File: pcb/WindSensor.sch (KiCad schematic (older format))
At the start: 13 parts, among them P1 SP, P2 0V, P3 3v3, P4 SP, P5 SDA, P6 SCL, P7 5V, P8 GND, P9 GND, U1 ArdinoMinPro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

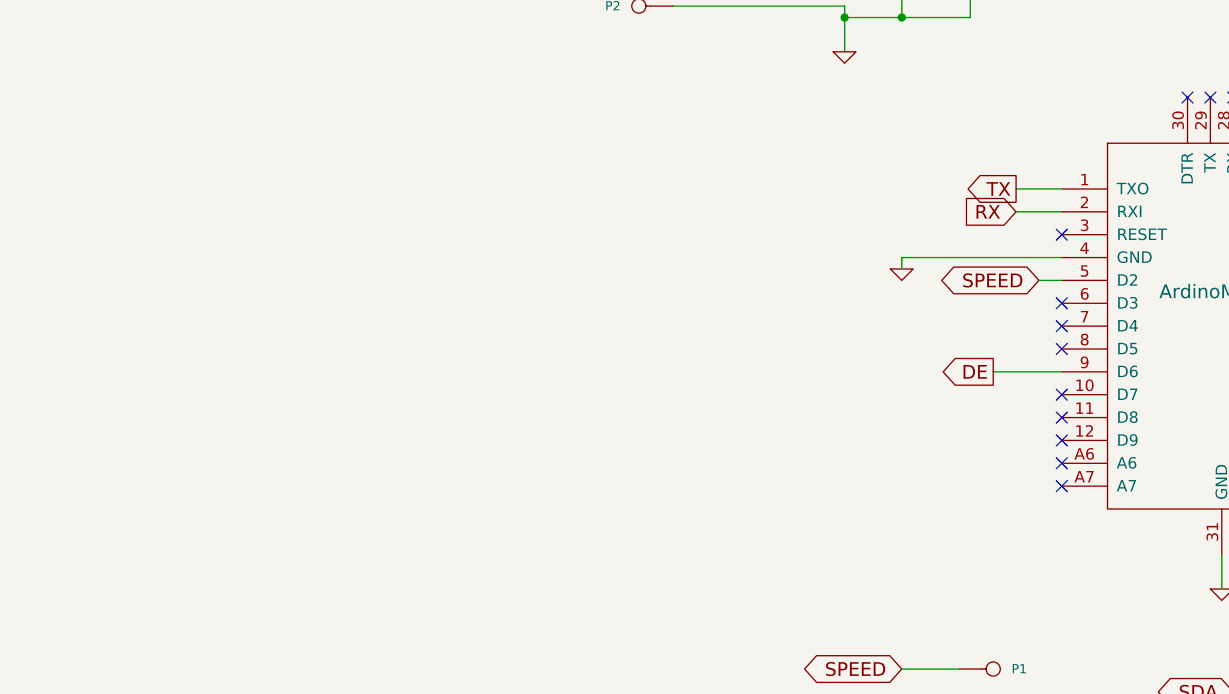
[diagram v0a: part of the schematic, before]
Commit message: Modularised the libraries and added unit tests, updated pcb, working version
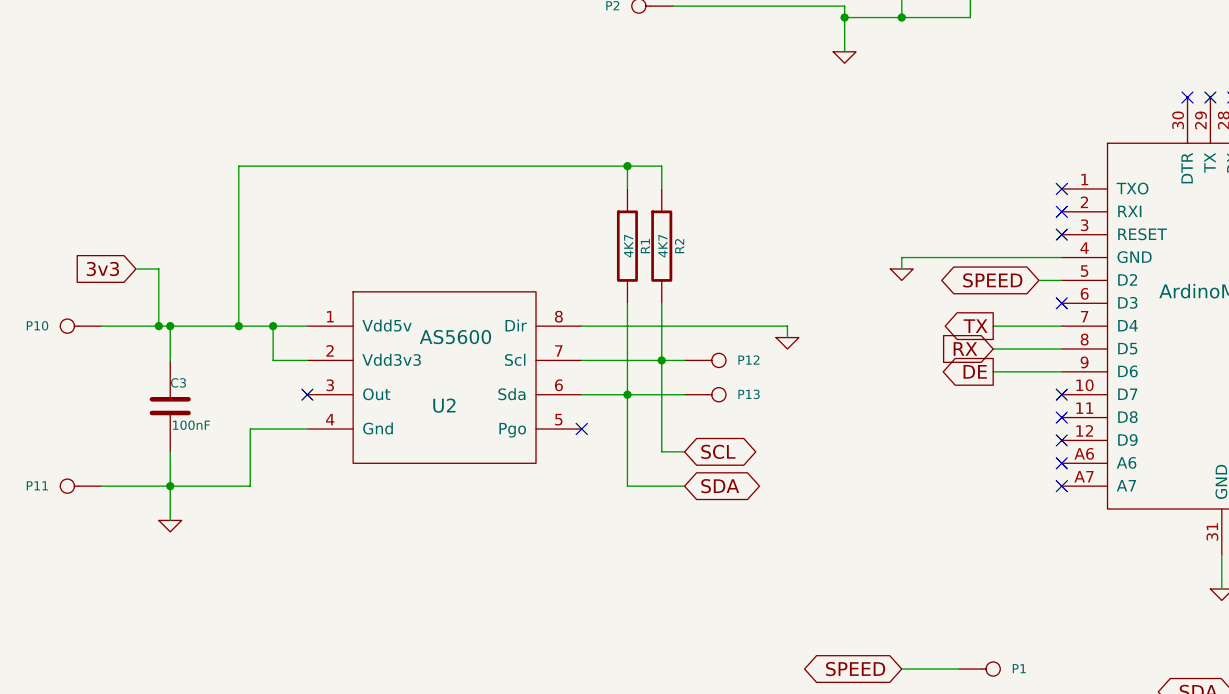
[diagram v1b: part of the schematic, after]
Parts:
- added C3: 100nF, Capacitors_SMD:C_0805, symbol C
- added P10: 3v3, Wire_Pads:SolderWirePad_single_0-8mmDrill, symbol CONN_1
- added P11: GND, Wire_Pads:SolderWirePad_single_0-8mmDrill, symbol CONN_1
- added P12: SDA, Wire_Pads:SolderWirePad_single_0-8mmDrill, symbol CONN_1
- added P13: SCL, Wire_Pads:SolderWirePad_single_0-8mmDrill, symbol CONN_1
- added R1, R2: 4K7, Capacitors_SMD:C_0805, symbol R
- added U2: AS5600, SMD_Packages:SOIC-8-N, symbol AS5600
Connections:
- net 3v3: now also C3.1, P10.1, R1.1, R2.1, U2.1 (Vdd5v), U2.2 (Vdd3v3)
- net GND: now also C3.2, P11.1, U2.4 (Gnd), U2.8 (Dir)
- net RX: now also U1.8 (D5); no longer U1.2 (RXI)
- net SCL: now also P12.1, R2.2, U2.7 (Scl)
- net SDA: now also P13.1, R1.2, U2.6 (Sda)
- net TX: now also U1.7 (D4); no longer U1.1 (TXO)
- no-connect marks 31 -> 33
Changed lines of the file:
@@
 Text GLabel 6750 4550 2    60   BiDi ~ 0
 SDA
-Text GLabel 4800 3350 0    60   Output ~ 0
+Text GLabel 4700 3950 0    60   Output ~ 0
 TX
-Text GLabel 4800 3450 0    60   Input ~ 0
+Text GLabel 4700 4050 0    60   Input ~ 0
 RX
 Text GLabel 4700 4150 0    60   Output ~ 0
@@
 NoConn ~ 5750 2950
 NoConn ~ 5850 2950
-NoConn ~ 5000 3950
-Wire Wire Line
-	6500 3450 6850 3450
-Wire Wire Line
-	6850 3450 6850 3500
-Wire Wire Line
-	4300 3650 5000 3650
-Wire Wire Line
-	6800 3650 6500 3650
-Wire Wire Line
-	5000 3750 4900 3750
-Wire Wire Line
-	4300 3650 4300 3700
-Wire Wire Line
-	6750 4550 6500 4550
-Wire Wire Line
-	6500 4650 6750 4650
-Wire Wire Line
-	9700 3500 9850 3500
-Wire Wire Line
-	9700 3600 9850 3600
-Wire Wire Line
-	9700 3200 10250 3200
-Wire Wire Line
-	9800 3200 9800 3300
-Wire Wire Line
-	9800 3300 9700 3300
-Wire Wire Line
-	9850 3400 9700 3400
-Wire Wire Line
-	9850 3700 9700 3700
-Wire Wire Line
-	10250 3200 10250 3300
-Connection ~ 9800 3200
-Wire Wire Line
-	6500 3350 6950 3350
-Wire Wire Line
-	4600 2600 4600 2450
-Wire Wire Line
-	4050 2600 4600 2600
-Wire Wire Line
-	4050 2550 4050 2750
-Wire Wire Line
-	4300 2450 4300 2600
-Connection ~ 4300 2600
-Wire Wire Line
-	3050 1900 4850 1900
-Wire Wire Line
-	4600 1900 4600 2050
-Wire Wire Line
-	4300 2050 4300 1900
-Connection ~ 4300 1900
-Wire Wire Line
-	3300 2550 4050 2550
-Connection ~ 4050 2600
-Wire Wire Line
-	6150 5250 6000 5250
-Connection ~ 4600 1900
-Wire Wire Line
-	6050 2950 6050 2850
-Wire Wire Line
-	5950 2850 6350 2850
-Wire Wire Line
-	6350 2850 6350 2950
-Wire Wire Line
-	5950 2850 5950 2950
-Connection ~ 6050 2850
-Wire Wire Line
-	5700 4950 5700 5100
-Wire Wire Line
-	5000 3450 4800 3450
-Wire Wire Line
-	5000 3350 4800 3350
 NoConn ~ 5000 3850
 $Comp
@@
 	1    0    0    -1
 $EndComp
-Wire Wire Line
-	4300 5450 4550 5450
 NoConn ~ 5000 4250
 $Comp
@@
 	1    0    0    -1
 $EndComp
-Wire Wire Line
-	4700 4150 5000 4150
-NoConn ~ 5000 4050
 Text GLabel 5750 5550 0    60   BiDi ~ 0
 SDA
@@
 	1    0    0    -1
 $EndComp
-Wire Wire Line
-	5750 5550 6000 5550
-Wire Wire Line
-	5750 5700 6000 5700
 $Comp
 L GND #PWR07
@@
 	1    0    0    -1
 $EndComp
-Wire Wire Line
-	5600 6050 5600 5950
-Wire Wire Line
-	5600 5950 6000 5950
 Text GLabel 4300 5650 0    60   Input ~ 0
 5V
@@
 	1    0    0    -1
 $EndComp
-Wire Wire Line
-	4300 5650 4550 5650
 $Comp
 L GND #PWR08
@@
 	1    0    0    -1
 $EndComp
+NoConn ~ 5000 3450
+NoConn ~ 5000 3350
+$Comp
+L AS5600 U2
+U 1 1 5FE9996D
+P 2300 4300
+F 0 "U2" H 2300 4300 60  0000 C CNN
+F 1 "AS5600" H 2350 4600 60  0000 C CNN
+F 2 "SMD_Packages:SOIC-8-N" H 2300 4300 60  0001 C CNN
+F 3 "" H 2300 4300 60  0001 C CNN
+	1    2300 4300
+	1    0    0    -1
+$EndComp
+Text GLabel 3350 4650 2    60   BiDi ~ 0
+SDA
+Text GLabel 3350 4500 2    60   BiDi ~ 0
+SCL
+NoConn ~ 1700 4250
+NoConn ~ 2900 4400
+$Comp
+L C C3
+U 1 1 5FE99E5F
+P 1100 4300
+F 0 "C3" H 1100 4400 40  0000 L CNN
+F 1 "100nF" H 1106 4215 40  0000 L CNN
+F 2 "Capacitors_SMD:C_0805" H 1138 4150 30  0001 C CNN
+F 3 "" H 1100 4300 60  0000 C CNN
+	1    1100 4300
+	1    0    0    -1
+$EndComp
+$Comp
+L GND #PWR09
+U 1 1 5FE99F11
+P 1100 4800
+F 0 "#PWR09" H 1100 4800 30  0001 C CNN
+F 1 "GND" H 1100 4730 30  0001 C CNN
+F 2 "" H 1100 4800 60  0001 C CNN
+F 3 "" H 1100 4800 60  0001 C CNN
+	1    1100 4800
+	1    0    0    -1
+$EndComp
+$Comp
+L R R2
+U 1 1 5FE9A09C
+P 3250 3600
+F 0 "R2" V 3330 3600 40  0000 C CNN
+F 1 "4K7" V 3257 3601 40  0000 C CNN
+F 2 "Capacitors_SMD:C_0805" V 3180 3600 30  0001 C CNN
+F 3 "" H 3250 3600 30  0000 C CNN
+	1    3250 3600
+	1    0    0    -1
+$EndComp
+$Comp
+L R R1
+U 1 1 5FE9A16A
+P 3100 3600
+F 0 "R1" V 3180 3600 40  0000 C CNN
+F 1 "4K7" V 3107 3601 40  0000 C CNN
+F 2 "Capacitors_SMD:C_0805" V 3030 3600 30  0001 C CNN
+F 3 "" H 3100 3600 30  0000 C CNN
+	1    3100 3600
+	1    0    0    -1
+$EndComp
+$Comp
+L GND #PWR010
+U 1 1 5FE9A1F6
+P 3800 4000
+F 0 "#PWR010" H 3800 4000 30  0001 C CNN
+F 1 "GND" H 3800 3930 30  0001 C CNN
+F 2 "" H 3800 4000 60  0001 C CNN
+F 3 "" H 3800 4000 60  0001 C CNN
+	1    3800 4000
+	1    0    0    -1
+$EndComp
+$Comp
+L CONN_1 P10
+U 1 1 5FE9A696
+P 650 3950
+F 0 "P10" H 730 3950 40  0000 L CNN
+F 1 "3v3" H 650 4005 30  0001 C CNN
+F 2 "Wire_Pads:SolderWirePad_single_0-8mmDrill" H 650 3950 60  0001 C CNN
+F 3 "" H 650 3950 60  0001 C CNN
+	1    650  3950
+	-1   0    0    1
+$EndComp
+Text GLabel 950  3700 0    60   Input ~ 0
+3v3
+$Comp
+L CONN_1 P12
+U 1 1 5FE9A6A0
+P 3500 4100
+F 0 "P12" H 3580 4100 40  0000 L CNN
+F 1 "SDA" H 3500 4155 30  0001 C CNN
+F 2 "Wire_Pads:SolderWirePad_single_0-8mmDrill" H 3500 4100 60  0001 C CNN
+F 3 "" H 3500 4100 60  0001 C CNN
+	1    3500 4100
+	1    0    0    -1
+$EndComp
+$Comp
+L CONN_1 P13
+U 1 1 5FE9A6A6
+P 3500 4250
+F 0 "P13" H 3580 4250 40  0000 L CNN
+F 1 "SCL" H 3500 4305 30  0001 C CNN
+F 2 "Wire_Pads:SolderWirePad_single_0-8mmDrill" H 3500 4250 60  0001 C CNN
+F 3 "" H 3500 4250 60  0001 C CNN
+	1    3500 4250
+	1    0    0    -1
+$EndComp
+$Comp
+L CONN_1 P11
+U 1 1 5FE9A6B4
+P 650 4650
+F 0 "P11" H 730 4650 40  0000 L CNN
+F 1 "GND" H 650 4705 30  0001 C CNN
+F 2 "Wire_Pads:SolderWirePad_single_0-8mmDrill" H 650 4650 60  0001 C CNN
+F 3 "" H 650 4650 60  0001 C CNN
+	1    650  4650
+	-1   0    0    1
+$EndComp
+Wire Wire Line
+	6500 3450 6850 3450
+Wire Wire Line
+	6850 3450 6850 3500
+Wire Wire Line
+	4300 3650 5000 3650
+Wire Wire Line
+	6800 3650 6500 3650
+Wire Wire Line
+	5000 3750 4900 3750
+Wire Wire Line
+	4300 3650 4300 3700
+Wire Wire Line
+	6750 4550 6500 4550
+Wire Wire Line
+	6500 4650 6750 4650
+Wire Wire Line
+	9700 3500 9850 3500
+Wire Wire Line
+	9700 3600 9850 3600
+Wire Wire Line
+	9700 3200 10250 3200
+Wire Wire Line
+	9800 3200 9800 3300
+Wire Wire Line
+	9800 3300 9700 3300
+Wire Wire Line
+	9850 3400 9700 3400
+Wire Wire Line
+	9850 3700 9700 3700
+Wire Wire Line
+	10250 3200 10250 3300
+Connection ~ 9800 3200
+Wire Wire Line
+	6500 3350 6950 3350
+Wire Wire Line
+	4600 2600 4600 2450
+Wire Wire Line
+	4050 2600 4600 2600
+Wire Wire Line
+	4050 2550 4050 2750
+Wire Wire Line
+	4300 2450 4300 2600
+Connection ~ 4300 2600
+Wire Wire Line
+	3050 1900 4850 1900
+Wire Wire Line
+	4600 1900 4600 2050
+Wire Wire Line
+	4300 2050 4300 1900
+Connection ~ 4300 1900
+Wire Wire Line
+	3300 2550 4050 2550
+Connection ~ 4050 2600
+Wire Wire Line
+	6150 5250 6000 5250
+Connection ~ 4600 1900
+Wire Wire Line
+	6050 2950 6050 2850
+Wire Wire Line
+	5950 2850 6350 2850
+Wire Wire Line
+	6350 2850 6350 2950
+Wire Wire Line
+	5950 2850 5950 2950
+Connection ~ 6050 2850
+Wire Wire Line
+	5700 4950 5700 5100
+Wire Wire Line
+	4300 5450 4550 5450
+Wire Wire Line
+	4700 4150 5000 4150
+Wire Wire Line
+	5750 5550 6000 5550
+Wire Wire Line
+	5750 5700 6000 5700
+Wire Wire Line
+	5600 6050 5600 5950
+Wire Wire Line
+	5600 5950 6000 5950
+Wire Wire Line
+	4300 5650 4550 5650
 Wire Wire Line
 	4550 5800 4200 5800
 Wire Wire Line
 	4200 5800 4200 5900
+Wire Wire Line
+	5000 4050 4700 4050
+Wire Wire Line
+	5000 3950 4700 3950
+Wire Wire Line
+	800  3950 1700 3950
+Wire Wire Line
+	1550 3950 1550 4100
+Wire Wire Line
+	1550 4100 1700 4100
+Wire Wire Line
+	1700 4400 1450 4400
+Wire Wire Line
+	1450 4400 1450 4650
+Wire Wire Line
+	1450 4650 800  4650
+Wire Wire Line
+	1100 4500 1100 4800
+Connection ~ 1100 4650
+Connection ~ 1550 3950
+Wire Wire Line
+	1100 4100 1100 3950
+Connection ~ 1100 3950
+Wire Wire Line
+	2900 3950 3800 3950
+Wire Wire Line
+	3800 3950 3800 4000
+Wire Wire Line
+	2900 4100 3350 4100
+Wire Wire Line
+	2900 4250 3350 4250
+Wire Wire Line
+	3100 3850 3100 4650
+Connection ~ 3100 4250
+Wire Wire Line
+	3250 3850 3250 4500
+Connection ~ 3250 4100
+Wire Wire Line
+	3250 3250 3250 3350
+Wire Wire Line
+	1400 3250 3250 3250
+Wire Wire Line
+	1400 3250 1400 3950
+Connection ~ 1400 3950
+Wire Wire Line
+	3100 3350 3100 3250
+Connection ~ 3100 3250
+Wire Wire Line
+	950  3700 1050 3700
+Wire Wire Line
+	1050 3700 1050 3950
+Connection ~ 1050 3950
+Wire Wire Line
+	3250 4500 3350 4500
+Wire Wire Line
+	3100 4650 3350 4650
 $EndSCHEMATC

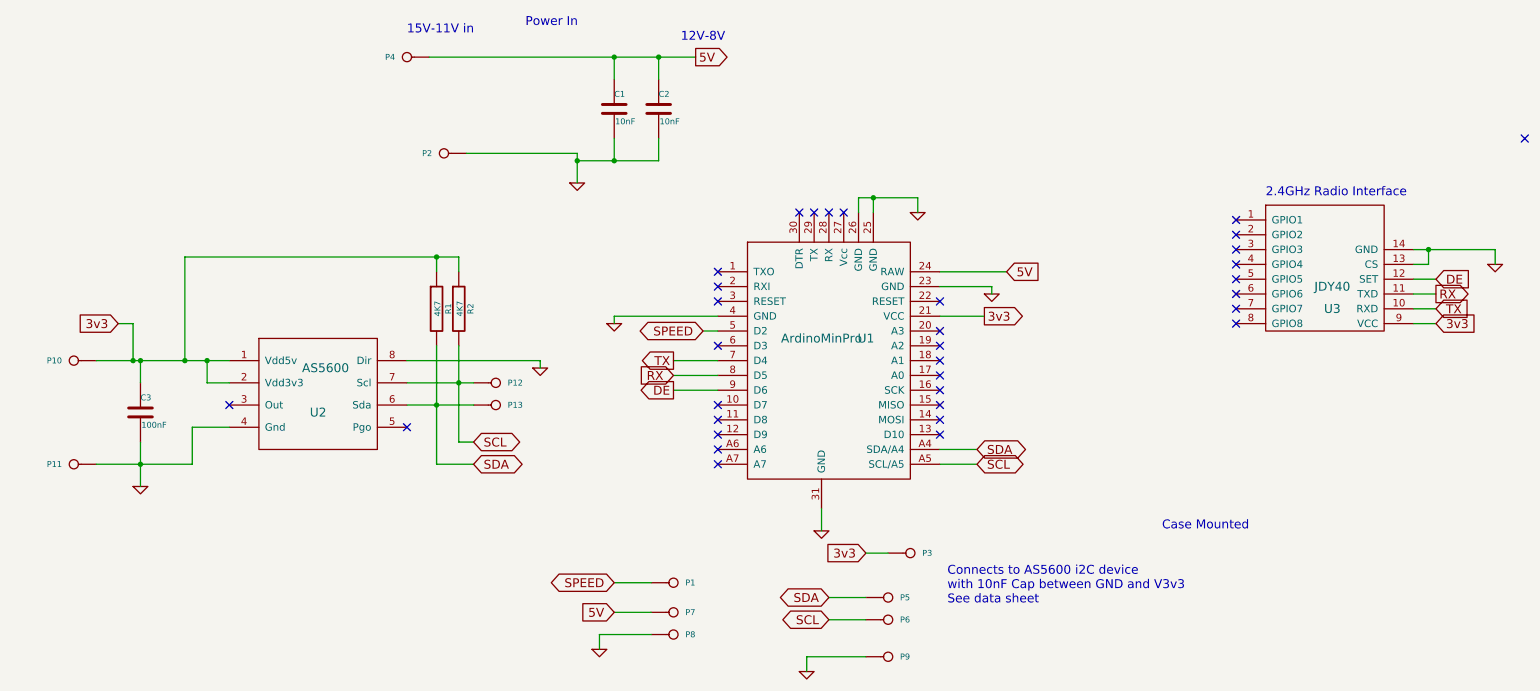
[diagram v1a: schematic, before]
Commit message: Switched to 3v hall device, fixed speed sensor to deal with pulse width variations
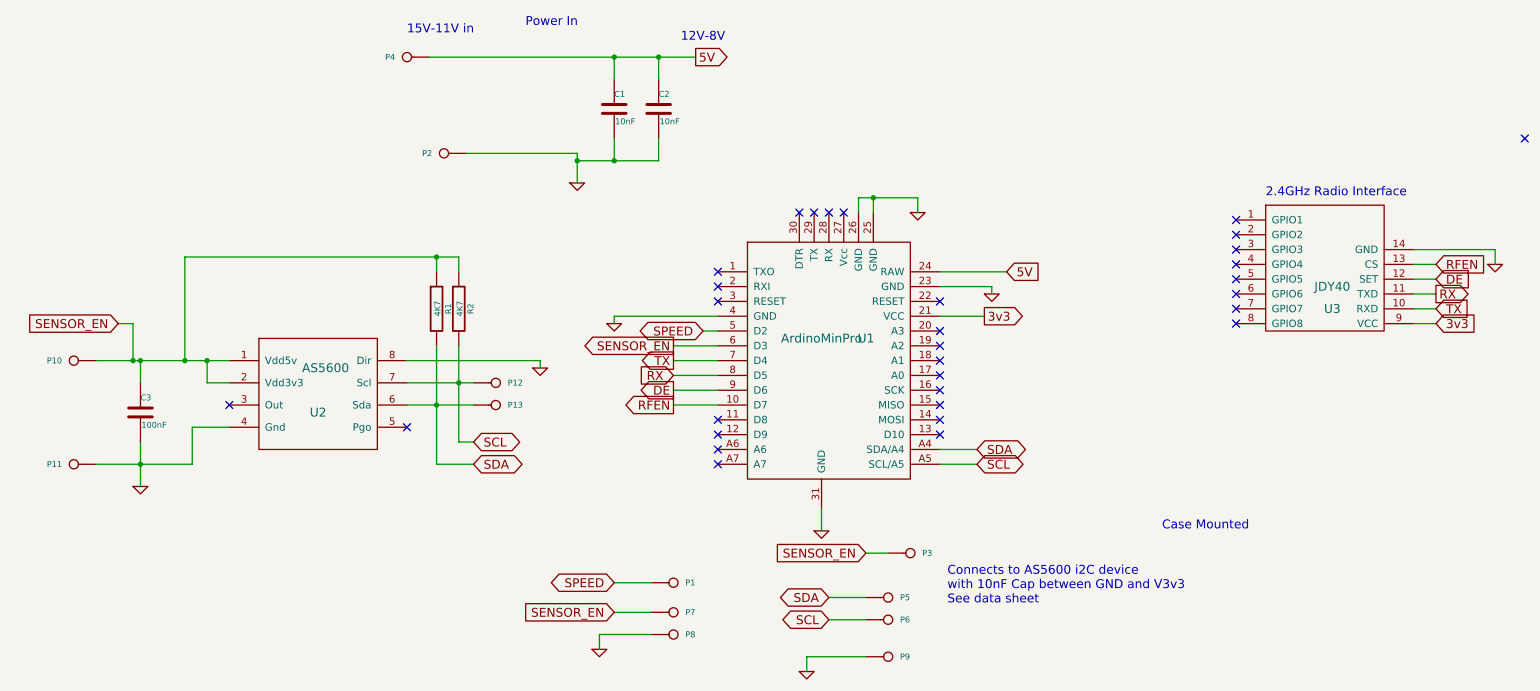
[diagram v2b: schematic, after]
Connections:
- net 3v3: no longer C3.1, P10.1, P3.1, R1.1, R2.1, U2.1 (Vdd5v), U2.2 (Vdd3v3)
- net 5V: no longer P7.1
- net GND: no longer U3.13 (CS)
- net RFEN: now reaches U1.10 (D7)
- net RFEN: now also U3.13 (CS)
- net SENSOR_EN: now reaches U1.6 (D3)
- net SENSOR_EN: now also C3.1, P10.1, P3.1, P7.1, R1.1, R2.1, U2.1 (Vdd5v), U2.2 (Vdd3v3)
- no-connect marks 33 -> 31
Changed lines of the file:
@@
 	1    0    0    -1
 $EndComp
-Text GLabel 6000 5250 0    60   Input ~ 0
-3v3
 Text Notes 6550 5600 0    60   ~ 0
 Connects to AS5600 i2C device\nwith 10nF Cap between GND and V3v3\nSee data sheet
@@
 NoConn ~ 5750 2950
 NoConn ~ 5850 2950
-NoConn ~ 5000 3850
 $Comp
 L CONN_1 P1
@@
 	1    0    0    -1
 $EndComp
-NoConn ~ 5000 4250
 $Comp
 L CONN_1 P4
@@
 	1    0    0    -1
 $EndComp
-Text GLabel 4300 5650 0    60   Input ~ 0
-5V
 $Comp
 L CONN_1 P7
@@
 	-1   0    0    1
 $EndComp
-Text GLabel 950  3700 0    60   Input ~ 0
-3v3
 $Comp
 L CONN_1 P12
@@
 	9700 3600 9850 3600
 Wire Wire Line
-	9700 3200 10250 3200
-Wire Wire Line
-	9800 3200 9800 3300
-Wire Wire Line
-	9800 3300 9700 3300
+	9700 3300 9850 3300
 Wire Wire Line
 	9850 3400 9700 3400
@@
 Wire Wire Line
 	10250 3200 10250 3300
-Connection ~ 9800 3200
 Wire Wire Line
 	6500 3350 6950 3350
@@
 	1700 4400 1450 4400
 Wire Wire Line
-	1450 4400 1450 4650
-Wire Wire Line
-	1450 4650 800  4650
+	1450 4650 1450 4400
+Wire Wire Line
+	800  4650 1450 4650
 Wire Wire Line
 	1100 4500 1100 4800
@@
 Wire Wire Line
 	3100 4650 3350 4650
+Text GLabel 4700 3850 0    60   Output ~ 0
+SENSOR_EN
+Wire Wire Line
+	4700 3850 5000 3850
+Text GLabel 6000 5250 0    60   Input ~ 0
+SENSOR_EN
+Text GLabel 950  3700 0    60   Input ~ 0
+SENSOR_EN
+Wire Wire Line
+	9700 3200 10250 3200
+Text GLabel 9850 3300 2    60   Input ~ 0
+RFEN
+Text GLabel 4700 4250 0    60   Output ~ 0
+RFEN
+Wire Wire Line
+	5000 4250 4700 4250
+Text GLabel 4300 5650 0    60   Input ~ 0
+SENSOR_EN
 $EndSCHEMATC
